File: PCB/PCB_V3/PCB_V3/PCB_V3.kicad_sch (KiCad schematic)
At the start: 84 parts, among them J1 ESP_Left, J10 MCP_RIGHT, J11 ACS2_pins, J12 Conn_01x03_Pin, J13 ACS2_Screw, J14 Screw_Terminal_01x02, J15 MCP_VCC_LINE, J16 AMS_IP_Pins, J17 AMS_OP_Pins, J18 BC1_IN+, J19 BC1_IN-, J2 ESP_Right, J20 BC3_IN+, J21 BC3_IN-, J22 BC1_OUT+, J23 BC1_OUT-, J24 BC3_OUT+, J25 BC3_OUT-, J26 BC2_IN+, J27 BC2_IN-, J28 BC5_IN+, J29 BC5_IN-, J3 ACS1_Pins, J30 BC2_OUT+, J31 BC2_OUT-, J32 BC5_OUT+, J33 BC5_OUT-, J34 Left_LED_1, J35 Left_LED_2, J36 Left_LED_3, J37 Left_LED_4, J38 Left_LED_5, J39 Right_LED_1, J4 ACS3_Pins, J40 Right_LED_2, J41 Right_LED_3, J42 Right_LED_4, J43 Right_LED_5, J44 STATIC_LED_1, J45 STATIC_LED_2, J46 I/P_Terminal, J47 Battery_Terminal, J5 ACS3_Screw, J6 ACS1_Screw, J7 LAN_Pins_2, J8 MCP_LEFT, J9 LAN_Pins_1, Q1 IRLZ44N, Q10 IRLZ44N, Q2 IRLZ44N, Q3 IRLZ44N, Q4 IRLZ44N, Q5 IRLZ44N, Q6 IRLZ44N, Q7 IRLZ44N, Q8 IRLZ44N, Q9 IRLZ44N

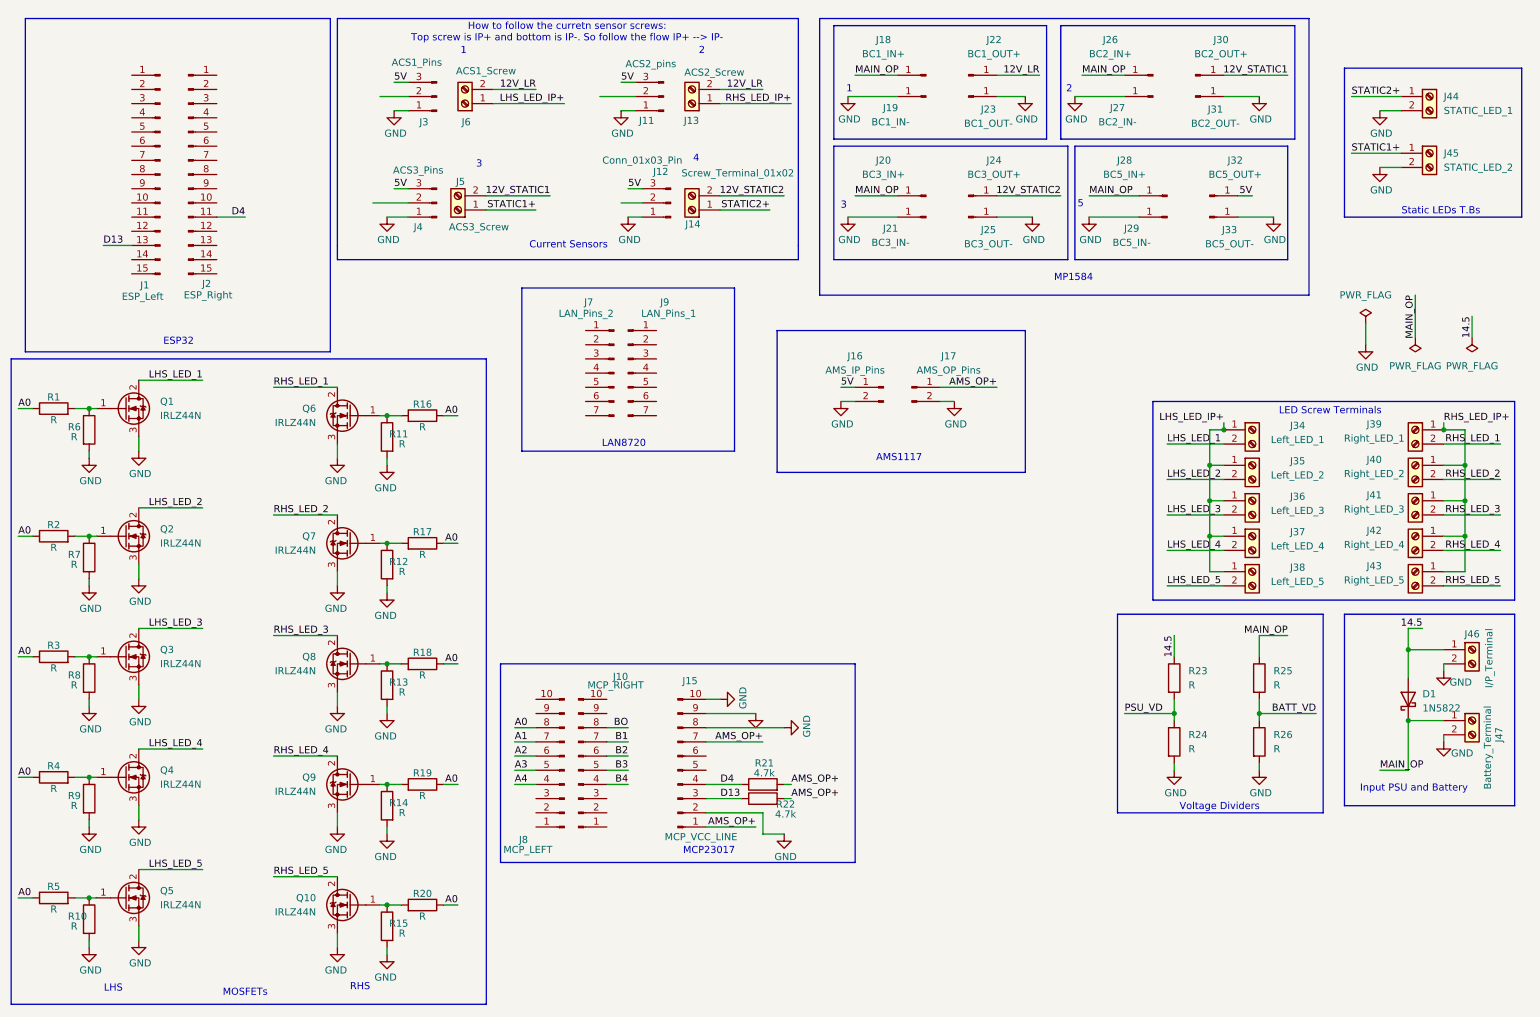
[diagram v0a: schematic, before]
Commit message: Committing the Final schematic file along with the
1. ESP32 connections made along with the LAN8720 module
2. Footprints assigned for all the individual components
3. Need to recheck and analyse the connections a 3rd and 4th time
5. Need to figure out component placement, on the PCB and close the tracing
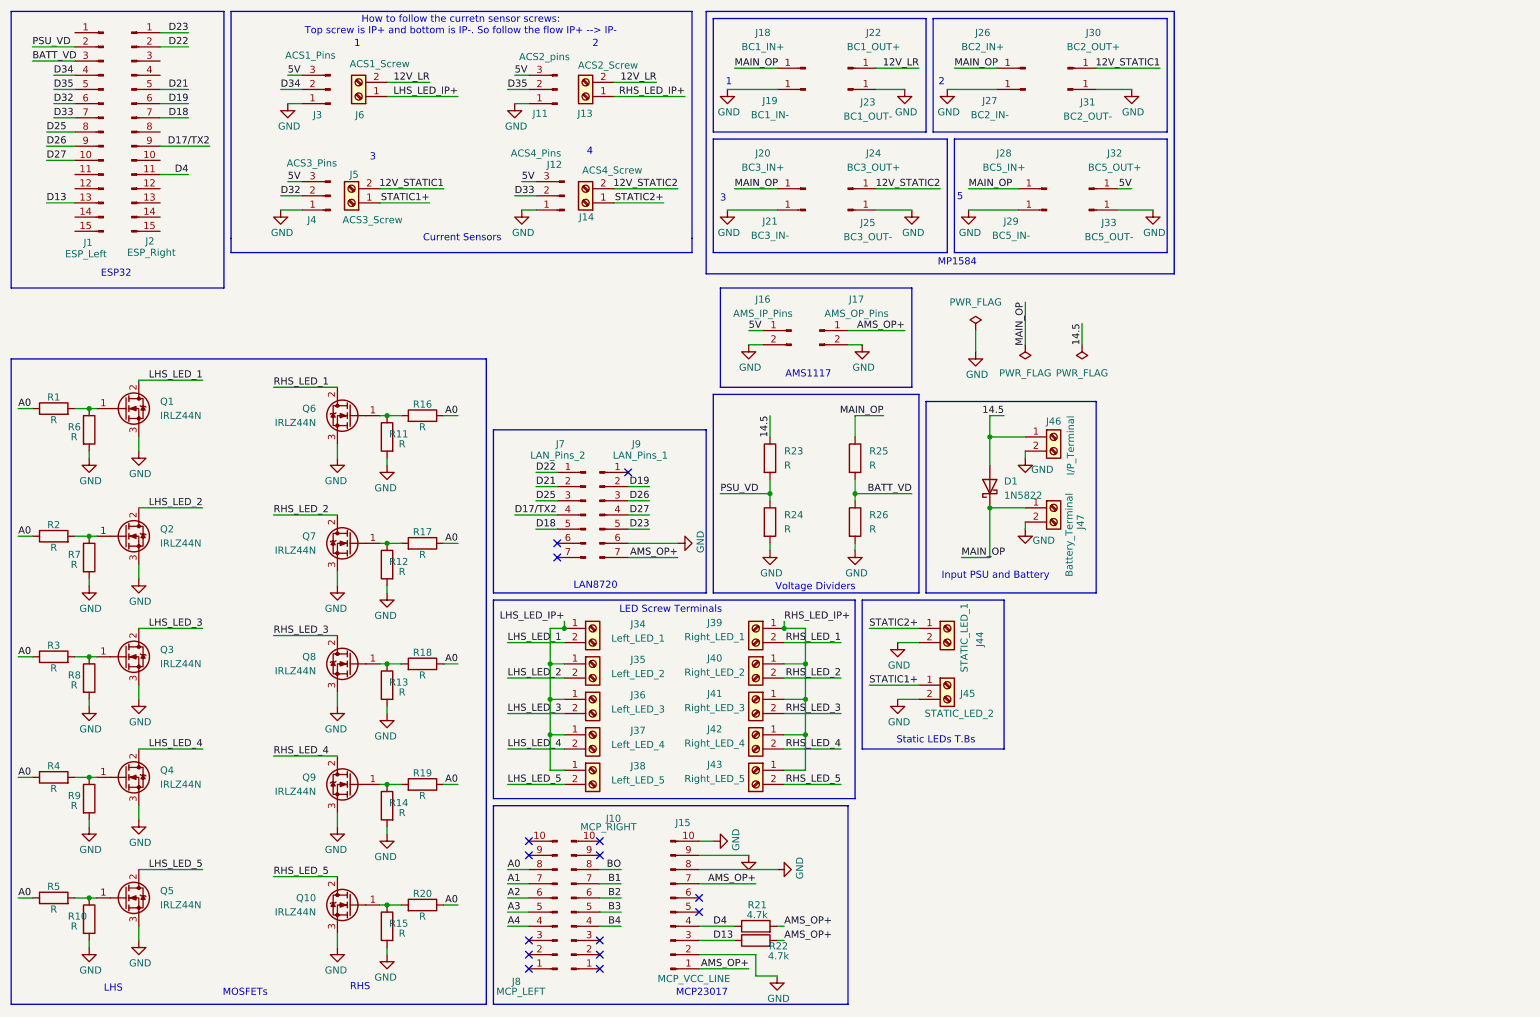
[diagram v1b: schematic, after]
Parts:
- J1, J2: footprint (none) -> Connector_PinHeader_2.54mm:PinHeader_1x15_P2.54mm_Vertical
- J10, J8: footprint (none) -> Connector_PinHeader_2.54mm:PinHeader_1x10_P2.54mm_Vertical
- J11: footprint (none) -> Connector_PinHeader_2.54mm:PinHeader_1x03_P2.54mm_Vertical
- J12: value Conn_01x03_Pin -> ACS4_Pins; footprint (none) -> Connector_PinSocket_2.54mm:PinSocket_1x03_P2.54mm_Vertical
- J13, J34, J35, J36, J37, J38, J39, J40, J41, J42, J43, J44, J45, J46, J47, J5, J6: footprint (none) -> TerminalBlock_Phoenix:TerminalBlock_Phoenix_MKDS-1,5-2-5.08_1x02_P5.08mm_Horizontal
- J14: value Screw_Terminal_01x02 -> ACS4_Screw; footprint (none) -> TerminalBlock_Phoenix:TerminalBlock_Phoenix_MKDS-1,5-2-5.08_1x02_P5.08mm_Horizontal
- J15: footprint (none) -> Connector_PinSocket_2.54mm:PinSocket_1x10_P2.54mm_Vertical
- J16, J17: footprint (none) -> Connector_PinSocket_2.54mm:PinSocket_1x02_P2.54mm_Vertical
- J18, J19, J20, J21, J22, J23, J24, J25, J26, J27, J28, J29, J30, J31, J32, J33: footprint (none) -> Connector_PinSocket_2.54mm:PinSocket_1x01_P2.54mm_Vertical
- J3, J4: footprint (none) -> Connector_PinSocket_2.54mm:PinSocket_1x03_P2.54mm_Vertical
- J7, J9: footprint (none) -> Connector_PinHeader_2.54mm:PinHeader_1x07_P2.54mm_Vertical
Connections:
- net AMS_OP+: now also J9.7 (Pin_7)
- net BATT_VD: now also J1.3 (Pin_3)
- net GND: now also J9.6 (Pin_6)
- net PSU_VD: now also J1.2 (Pin_2)
- net D34: now reaches J3.2 (Pin_2)
- net D34: now also J1.4 (Pin_4)
- net D27: now reaches J1.10 (Pin_10)
- net D27: now also J9.4 (Pin_4)
- net D35: now reaches J1.5 (Pin_5)
- net D35: now also J11.2 (Pin_2)
- net D32: now reaches J1.6 (Pin_6)
- net D32: now also J4.2 (Pin_2)
- net D33: now reaches J1.7 (Pin_7)
- net D33: now also J12.2 (Pin_2)
- net D25: now reaches J1.8 (Pin_8)
- net D25: now also J7.3 (Pin_3)
- net D26: now reaches J1.9 (Pin_9)
- net D26: now also J9.3 (Pin_3)
- net D19: now reaches J9.2 (Pin_2)
- net D19: now also J2.6 (Pin_6)
- net D23: now reaches J9.5 (Pin_5)
- net D23: now also J2.1 (Pin_1)
- net D22: now reaches J7.1 (Pin_1)
- net D22: now also J2.2 (Pin_2)
- net D21: now reaches J7.2 (Pin_2)
- net D21: now also J2.5 (Pin_5)
- net D17/TX2: now reaches J7.4 (Pin_4)
- net D17/TX2: now also J2.9 (Pin_9)
- net D18: now reaches J7.5 (Pin_5)
- net D18: now also J2.7 (Pin_7)
- no-connect marks 0 -> 15
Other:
- moved on the sheet: D1, J1, J10, J11, J12, J13, J14, J15, J16, J17, J18, J19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
